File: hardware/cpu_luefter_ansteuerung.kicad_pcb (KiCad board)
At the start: 2 copper layers, 50.8 x 67.3 mm, 29 parts, among them J1 Power 12V DC, J2 ISP, J3 CPU Lüfter, Q1 BC337, SW1 SW_Push, U1 7805, U2 ATtiny24A-PU, U3 74HC595, U4 KCSA02-123

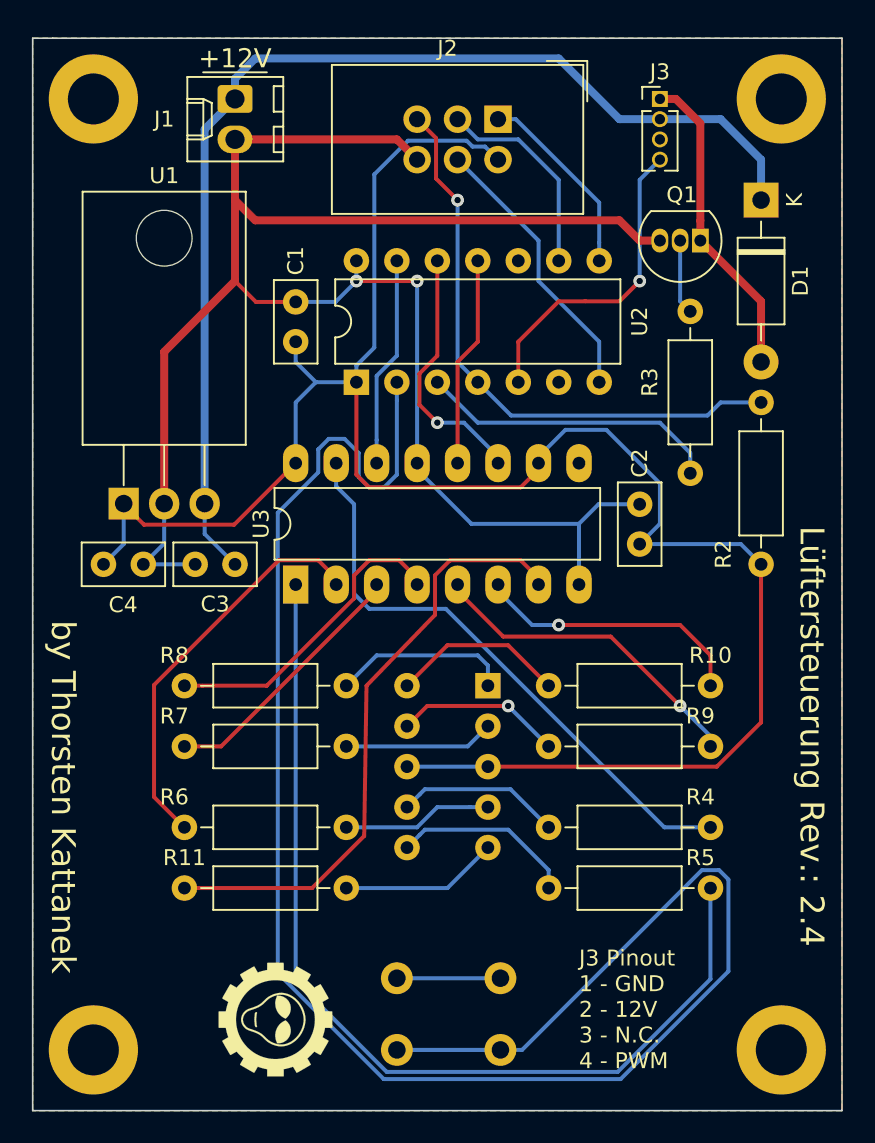
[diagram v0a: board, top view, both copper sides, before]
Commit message: Shematic und PCB für 7805 korrigiert. Neue Gerber Dateien erzeugt
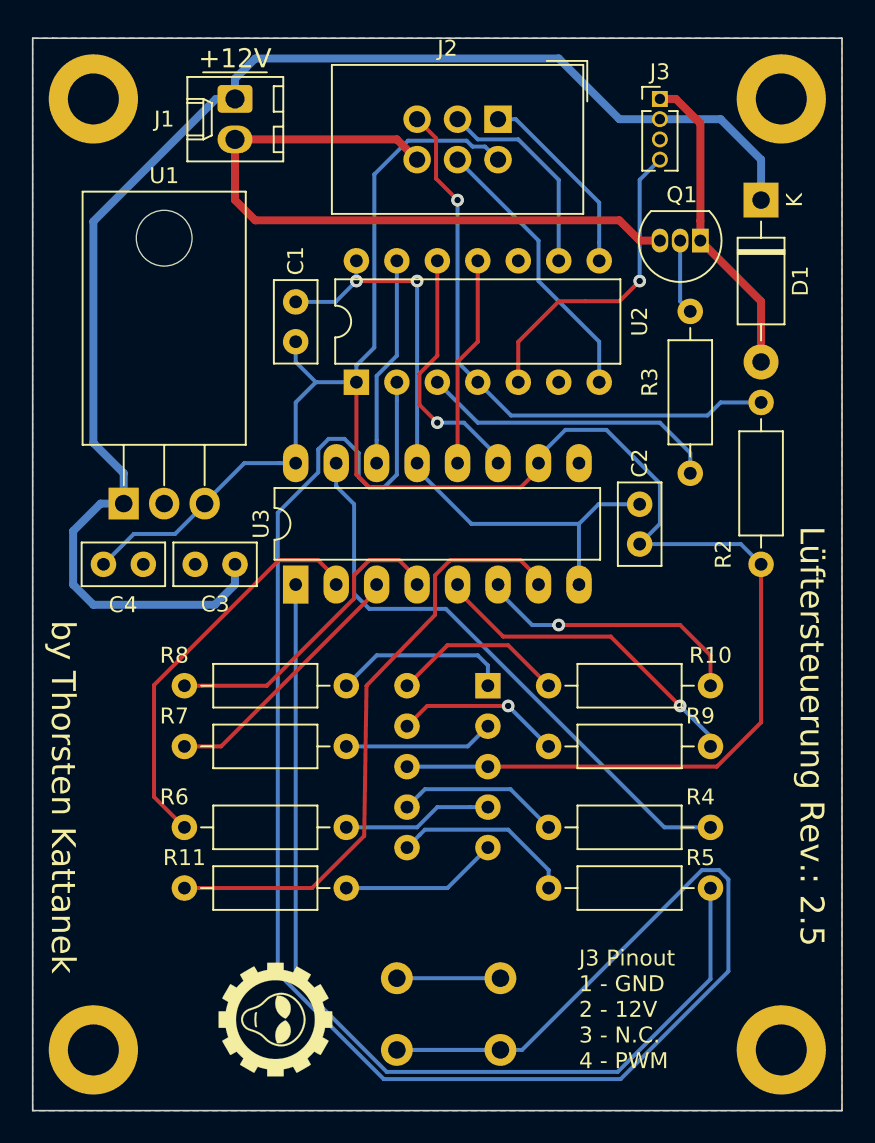
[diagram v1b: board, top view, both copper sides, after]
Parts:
- U1: value 7805 -> L7805
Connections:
- U1 pad 1: +5V -> +12V
- U1 pad 3: +12V -> +5V
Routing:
- net GND: track 123.8 -> 91.0 mm
- net +12V: track 70.8 -> 90.3 mm
- net +5V: track 125.5 -> 122.9 mm
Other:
- board text added: "Lüftersteuerung Rev.: 2.5"
- board text removed: "Lüftersteuerung Rev.: 2.4"

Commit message: J3 Footprint geändert
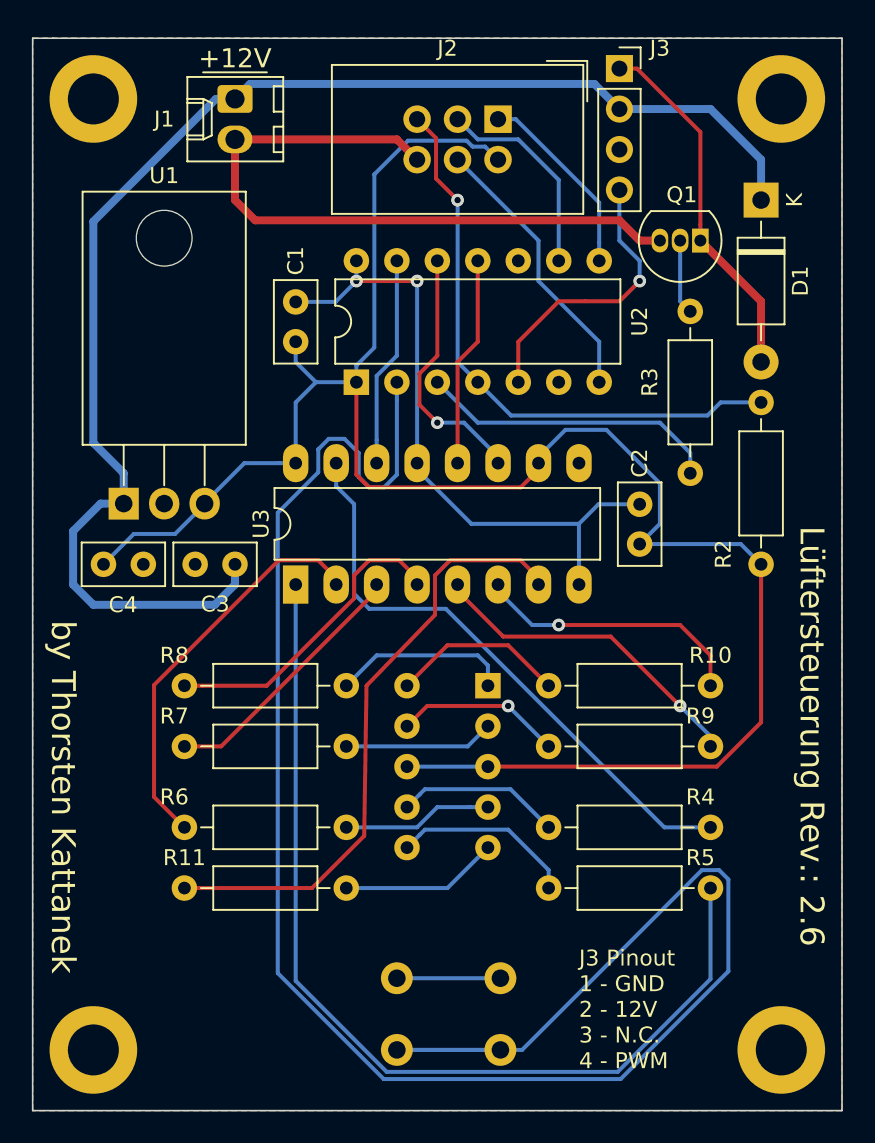
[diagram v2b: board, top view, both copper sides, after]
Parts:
- removed G***: LOGO, Kattanek Logo:logo_01_7_1mm_fsilk
- removed the REF** at (148.6, 135.9)
- removed the REF** at (105.4, 135.9)
- removed the REF** at (148.6, 76.2)
- removed the REF** at (105.4, 76.2)
- added REF**: MountingHole_3.2mm_M3_ISO14580_Pad, MountingHole:MountingHole_3.2mm_M3_ISO14580_Pad, F.Cu at (148.6, 76.2)
- added REF**: MountingHole_3.2mm_M3_ISO14580_Pad, MountingHole:MountingHole_3.2mm_M3_ISO14580_Pad, F.Cu at (148.6, 135.9)
- added REF**: MountingHole_3.2mm_M3_ISO14580_Pad, MountingHole:MountingHole_3.2mm_M3_ISO14580_Pad, F.Cu at (105.4, 135.9)
- added REF**: MountingHole_3.2mm_M3_ISO14580_Pad, MountingHole:MountingHole_3.2mm_M3_ISO14580_Pad, F.Cu at (105.4, 76.2)
- J3: footprint Connector_PinHeader_1.27mm:PinHeader_1x04_P1.27mm_Vertical -> Connector_PinSocket_2.54mm:PinSocket_1x04_P2.54mm_Vertical
- moved J3 3.17 mm to (138.4, 74.3)
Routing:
- net Net-(D1-Pad2): track 19.7 -> 22.7 mm
- net +12V: track 90.3 -> 88.3 mm
- net FAN_PWM: track 19.9 -> 18.0 mm
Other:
- board text added: "Lüftersteuerung Rev.: 2.6"
- board text removed: "Lüftersteuerung Rev.: 2.5"

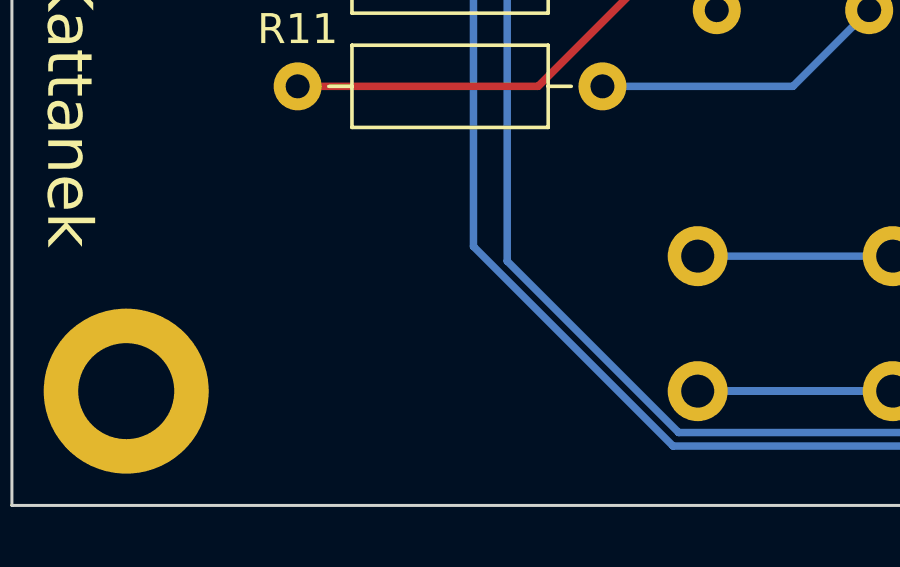
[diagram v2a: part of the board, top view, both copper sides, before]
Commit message: Logo wieder eingefügt
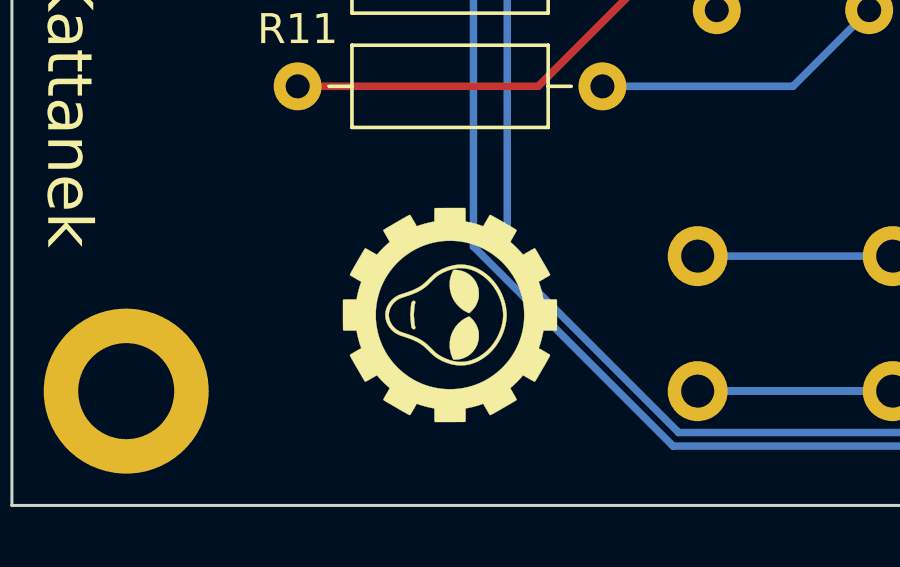
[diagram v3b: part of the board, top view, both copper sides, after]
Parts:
- added G***: LOGO, Kattanek Logo:logo_01_7_1mm_fsilk, F.Cu at (116.2, 133.3)
